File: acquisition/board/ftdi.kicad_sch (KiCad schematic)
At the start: 2 parts, among them U10 FT232HL, U6 ICE40UP5K_QFN48

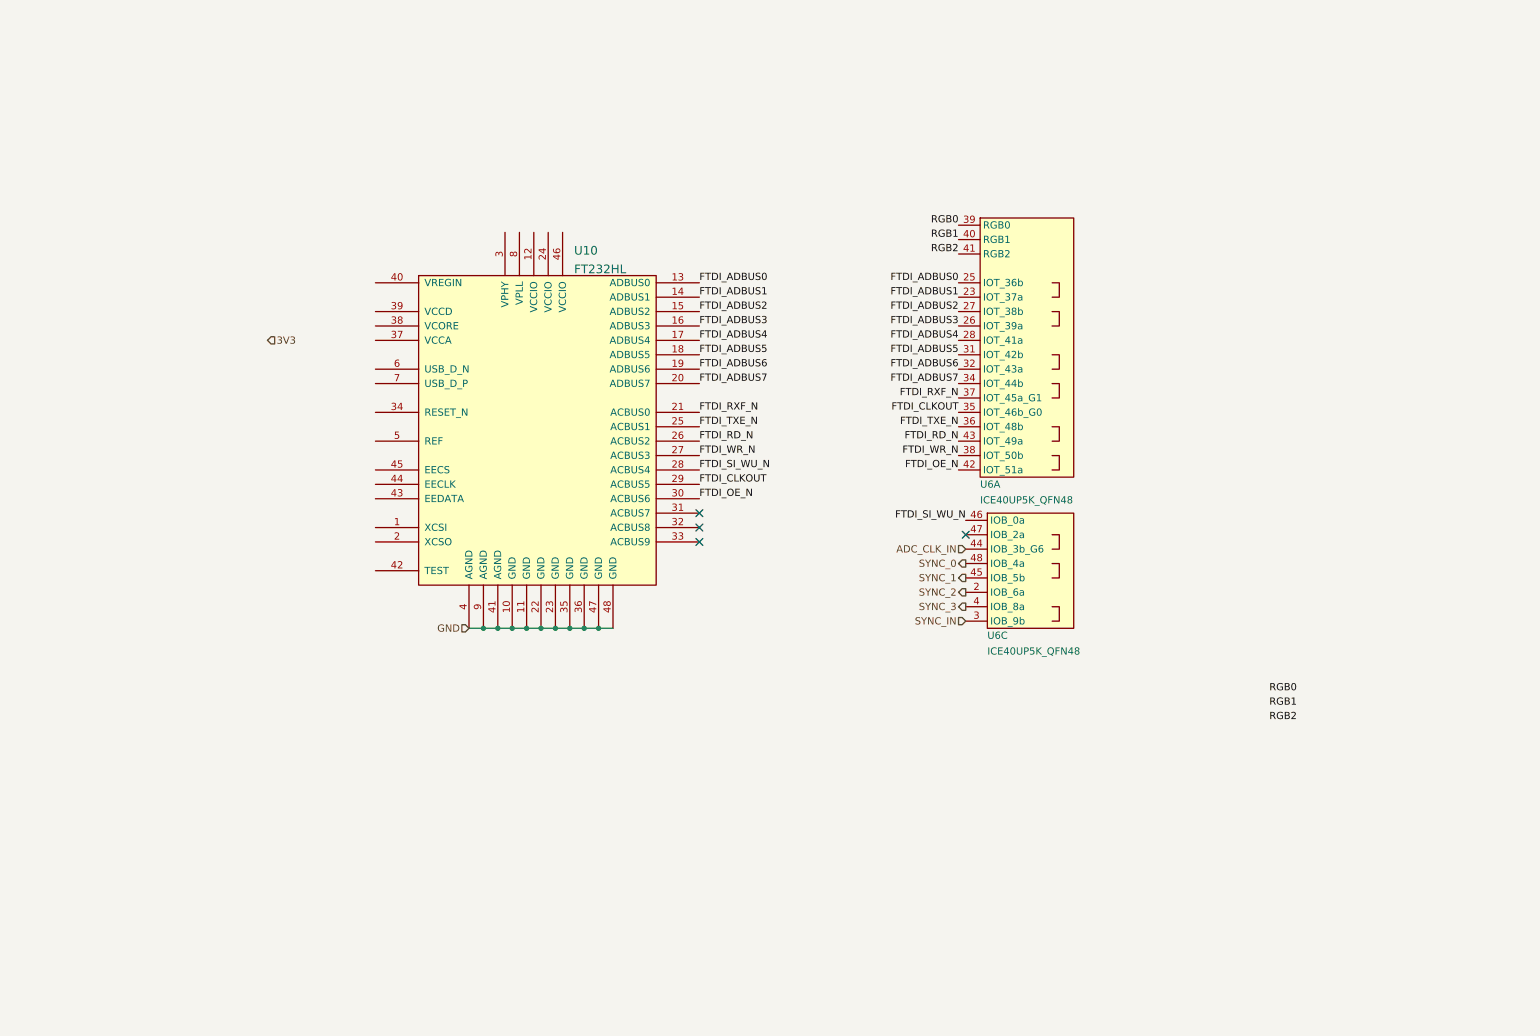
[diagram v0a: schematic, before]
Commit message: Updated schematic with a lot of level shifting and support stuff, power decoupling, etc. Almost done except power supply and protection diodes
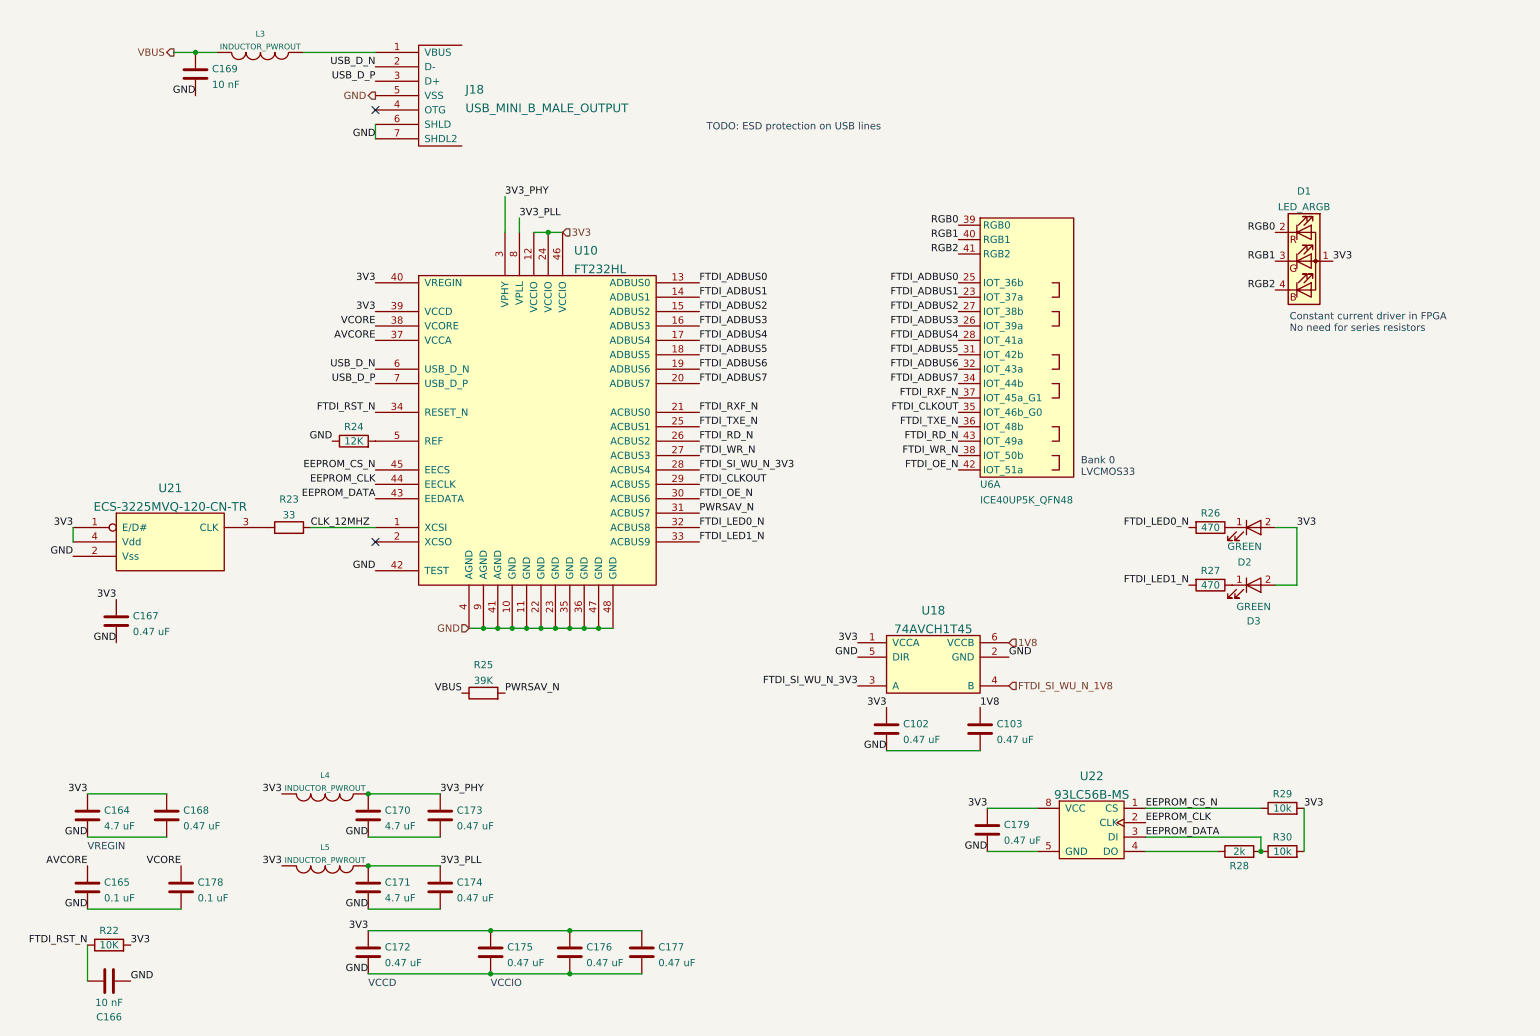
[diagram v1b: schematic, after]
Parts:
- removed unit 3 of U6
- added C102, C103, C167, C168, C172, C173, C174, C175, C176, C177, C179: 0.47 uF, symbol device:C
- added C164, C170, C171: 4.7 uF, symbol device:C
- added C165, C178: 0.1 uF, symbol device:C
- added C166, C169: 10 nF, symbol device:C
- added D1: LED_ARGB, symbol device:LED_ARGB
- added D2, D3: GREEN, symbol device:LED
- added J18: USB_MINI_B_MALE_OUTPUT, symbol special-azonenberg:USB_MINI_B_MALE_OUTPUT
- added L3, L4, L5: INDUCTOR_PWROUT, symbol passive-azonenberg:INDUCTOR_PWROUT
- added R22: 10K, symbol device:R
- added R23: 33, symbol device:R
- added R24: 12K, symbol device:R
- added R25: 39K, symbol device:R
- added R26, R27: 470, symbol device:R
- added R28: 2k, symbol device:R
- added R29, R30: 10k, symbol device:R
- added U18: 74AVCH1T45, symbol special-azonenberg:74LVC1T45
- added U21: ECS-3225MVQ-120-CN-TR, symbol osc-azonenberg:OSC
- added U22: 93LC56B-MS, symbol memory-azonenberg:93LC56B-MS
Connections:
- net 3V3: now also U10.12 (VCCIO), U10.24 (VCCIO), U10.39 (VCCD), U10.40 (VREGIN), U10.46 (VCCIO), C102.1, C164.1, C167.1, C168.1, C172.1, C175.1, C176.1, C177.1, C179.1, D1.1 (A), D2.2 (A), D3.2 (A), L4.2, L5.2, R22.2, R29.2, R30.2, U18.1 (VCCA), U21.1 (E/D#), U21.4 (Vdd), U22.8 (VCC)
- net GND: now also U10.42 (TEST), C102.2, C103.2, C164.2, C165.2, C166.2, C167.2, C168.2, C169.2, C170.2, C171.2, C172.2, C173.2, C174.2, C175.2, C176.2, C177.2, C178.2, C179.2, J18.5 (VSS), J18.6 (SHLD), J18.7 (SHDL2), R24.1, U18.2 (GND), U18.5 (DIR), U21.2 (Vss), U22.5 (GND)
- net RGB0: now also D1.2 (RK)
- net RGB1: now also D1.3 (GK)
- net RGB2: now also D1.4 (BK)
- net CLK_12MHZ: now reaches U10.1 (XCSI)
- net CLK_12MHZ: now also R23.2
- net 3V3_PHY: now reaches U10.3 (VPHY)
- net 3V3_PHY: now also C170.1, C173.1, L4.1
- net PWRSAV_N: now reaches U10.31 (ACBUS7)
- net PWRSAV_N: now also R25.2
- net FTDI_LED0_N: now reaches U10.32 (ACBUS8)
- net FTDI_LED0_N: now also R26.2
- net FTDI_LED1_N: now reaches U10.33 (ACBUS9)
- net FTDI_LED1_N: now also R27.2
- net FTDI_RST_N: now reaches U10.34 (RESET_N)
- net FTDI_RST_N: now also C166.1, R22.1
- net AVCORE: now reaches U10.37 (VCCA)
- net AVCORE: now also C165.1
- net VCORE: now reaches U10.38 (VCORE)
- net VCORE: now also C178.1
- net EEPROM_DATA: now reaches U10.43 (EEDATA)
- net EEPROM_DATA: now also R28.2, R30.1, U22.3 (DI)
- net EEPROM_CLK: now reaches U10.44 (EECLK)
- net EEPROM_CLK: now also U22.2 (CLK)
- net EEPROM_CS_N: now reaches U10.45 (EECS)
- net EEPROM_CS_N: now also R29.1, U22.1 (CS)
- net at U10.5 (REF): now also R24.2
- net USB_D_N: now reaches U10.6 (USB_D_N)
- net USB_D_N: now also J18.2 (D-)
- net USB_D_P: now reaches U10.7 (USB_D_P)
- net USB_D_P: now also J18.3 (D+)
- net 3V3_PLL: now reaches U10.8 (VPLL)
- net 3V3_PLL: now also C171.1, C174.1, L5.1
- net FTDI_SI_WU_N renamed FTDI_SI_WU_N_3V3
- net FTDI_SI_WU_N_3V3: now also U18.3 (A)
- new net: D2.1 (K), R26.1
- new net: R23.1, U21.3 (CLK)
- new net: R28.1, U22.4 (DO)
- new net: J18.1 (VBUS), L3.1
- new net: D3.1 (K), R27.1
- new net 1V8: C103.1, U18.6 (VCCB)
- new net FTDI_SI_WU_N_1V8: U18.4 (B)
- new net VBUS: C169.1, L3.2, R25.1
- no-connect marks 4 -> 2
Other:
- note added: "Bank 0 LVCMOS33"
- note added: "Constant current driver in FPGA No need for series resistors"
- note added: "TODO: ESD protection on USB lines"
- note added: "VCCD"
- note added: "VCCIO"
- note added: "VREGIN"

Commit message: Lots of progress on power supply design, added a bunch of test points, etc
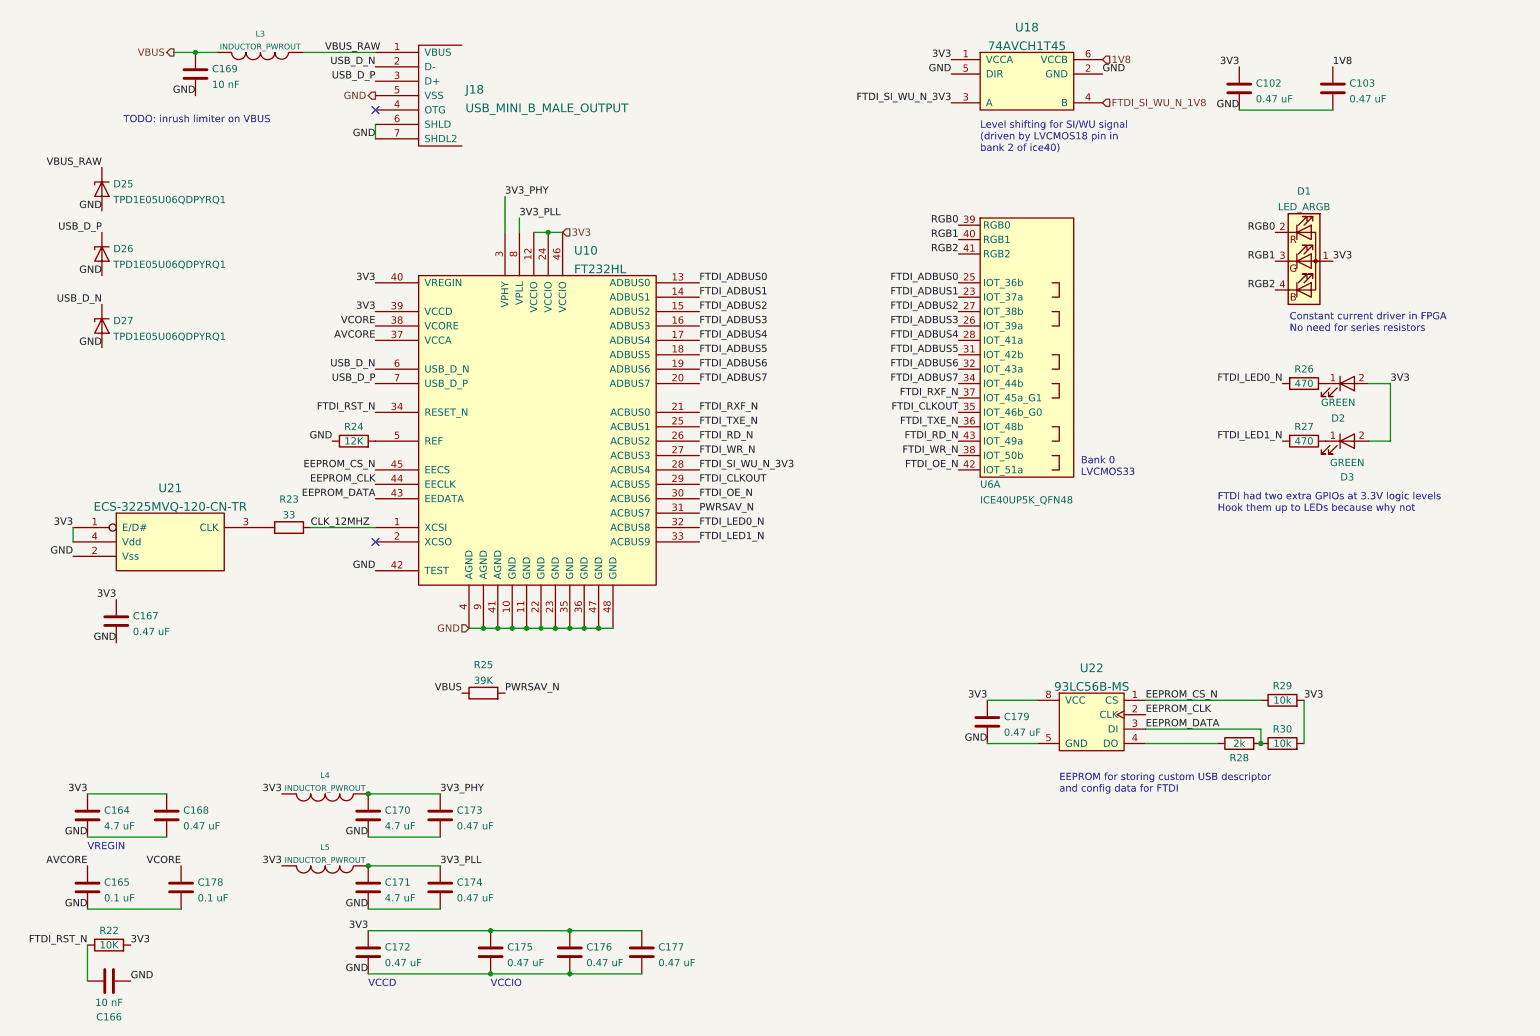
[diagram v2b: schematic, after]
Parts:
- added D25, D26, D27: TPD1E05U06QDPYRQ1, symbol device:D_Zener
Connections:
- net GND: now also D25.2 (A), D26.2 (A), D27.2 (A)
- net USB_D_N: now also D27.1 (K)
- net USB_D_P: now also D26.1 (K)
- net VBUS_RAW: now reaches J18.1 (VBUS), L3.1
- net VBUS_RAW: now also D25.1 (K)
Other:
- note added: "EEPROM for storing custom USB descriptor and config data for FTDI"
- note added: "FTDI had two extra GPIOs at 3.3V logic levels Hook them up to LEDs because why not"
- note added: "Level shifting for SI/WU signal (driven by LVCMOS18 pin in bank 2 of ice40)"
- note added: "TODO: inrush limiter on VBUS"
- note removed: "TODO: ESD protection on USB lines"
- moved on the sheet: C102, C103, C179, D2, D3, R26, R27, R28, R29, R30, U18, U22

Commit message: More power supply work, added PLL loop filter, soft start, began assigning footprints
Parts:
- removed J18: USB_MINI_B_MALE_OUTPUT, symbol special-azonenberg:USB_MINI_B_MALE_OUTPUT
- added C220: 4.7 uF, azonenberg_pcb:EIA_0603_CAP_NOSILK, symbol device:C
- added J18: UX60SX-MB-5ST, azonenberg_pcb:CONN_HIROSE_UX60S-MB-5ST_MINI_USB, symbol hirose-azonenberg:HIROSE_UX60SX-MB-5ST_(MINI_USB)
- added U29: SIP32408, symbol power-azonenberg:SIP32408
- C102, C103, C165, C167, C168, C172, C173, C174, C175, C176, C177, C178, C179: footprint (none) -> azonenberg_pcb:EIA_0402_CAP_NOSILK
- L3, L4, L5: value INDUCTOR_PWROUT -> FERRITE
- R22, R23, R26, R27, R29, R30: footprint (none) -> azonenberg_pcb:EIA_0402_RES_NOSILK
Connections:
- net GND: now also C220.2, J18.5 (VSS), J18.6 (SHLD), J18.7 (SHDL2), U29.2 (GND), U29.PAD (GND)
- net USB_D_N: now also J18.2 (D-)
- net USB_D_P: now also J18.3 (D+)
- net VBUS: now also U29.4 (OUT); no longer L3.2
- net VBUS_RAW: now also L3.2, J18.1 (VBUS); no longer L3.1
- new net VBUS_FILT: C220.1, L3.1, U29.1 (IN), U29.3 (EN)
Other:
- note added: "Inrush limiter 2.5 ms turn-on ramp"
- note removed: "TODO: inrush limiter on VBUS"
- moved on the sheet: C169, L3

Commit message: Completed schematic after design review, ready for layout
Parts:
- added R85, R86, R87, R88: 33, azonenberg_pcb:EIA_0402_RES_NOSILK, symbol device:R
- C164, C166, C169, C170, C171: footprint (none) -> azonenberg_pcb:EIA_0603_CAP_NOSILK
- R24, R25, R28: footprint (none) -> azonenberg_pcb:EIA_0402_RES_NOSILK
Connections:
- net FTDI_CLKOUT: now also R88.2; no longer U10.29 (ACBUS5)
- net FTDI_OE_N: now also R87.1; no longer U6.42 (IOT_51a)
- net FTDI_RD_N: now also R85.1; no longer U6.43 (IOT_49a)
- net FTDI_WR_N: now also R86.1; no longer U6.38 (IOT_50b)
- new net: R85.2, U6.43 (IOT_49a)
- new net: R86.2, U6.38 (IOT_50b)
- new net: R87.2, U6.42 (IOT_51a)
- new net: R88.1, U10.29 (ACBUS5)
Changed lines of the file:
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@@
   (title_block
     (title "Digitizer board")
-    (date "2022-07-08")
+    (date "2022-07-17")
     (rev "0.1")
     (company "A. Zonenberg")
@@
     (stroke (width 0) (type default) (color 0 0 0 0))
   )
+  (wire (pts (xy 144.78 96.52) (xy 148.59 96.52))
+    (stroke (width 0) (type default) (color 0 0 0 0))
+  )
   (wire (pts (xy 110.49 52.07) (xy 113.03 52.07))
     (stroke (width 0) (type default) (color 0 0 0 0))
@@
     (stroke (width 0) (type default) (color 0 0 0 0))
   )
+  (wire (pts (xy 170.18 88.9) (xy 175.26 88.9))
+    (stroke (width 0) (type default) (color 0 0 0 0))
+  )
   (wire (pts (xy 215.9 142.24) (xy 228.6 142.24))
     (stroke (width 0) (type default) (color 0 0 0 0))
@@
     (stroke (width 0) (type default) (color 0 0 0 0))
   )
+  (wire (pts (xy 170.18 91.44) (xy 175.26 91.44))
+    (stroke (width 0) (type default) (color 0 0 0 0))
+  )
   (wire (pts (xy 187.96 134.62) (xy 196.85 134.62))
     (stroke (width 0) (type default) (color 0 0 0 0))
   )
   (wire (pts (xy 78.74 158.75) (xy 91.44 158.75))
+    (stroke (width 0) (type default) (color 0 0 0 0))
+  )
+  (wire (pts (xy 170.18 93.98) (xy 175.26 93.98))
     (stroke (width 0) (type default) (color 0 0 0 0))
   )
@@
     (effects (font (size 1.27 1.27)) (justify left bottom))
   )
-  (label "FTDI_RD_N" (at 182.88 88.9 180)
+  (label "FTDI_RD_N" (at 170.18 88.9 180)
     (effects (font (size 1.27 1.27)) (justify right bottom))
   )
@@
     (effects (font (size 1.27 1.27)) (justify right bottom))
   )
-  (label "FTDI_CLKOUT" (at 137.16 96.52 0)
+  (label "FTDI_CLKOUT" (at 148.59 96.52 0)
     (effects (font (size 1.27 1.27)) (justify left bottom))
   )
@@
     (effects (font (size 1.27 1.27)) (justify right bottom))
   )
-  (label "FTDI_WR_N" (at 182.88 91.44 180)
+  (label "FTDI_WR_N" (at 170.18 91.44 180)
     (effects (font (size 1.27 1.27)) (justify right bottom))
   )
@@
     (effects (font (size 1.27 1.27)) (justify left bottom))
   )
-  (label "FTDI_OE_N" (at 182.88 93.98 180)
+  (label "FTDI_OE_N" (at 170.18 93.98 180)
     (effects (font (size 1.27 1.27)) (justify right bottom))
   )
@@
     (pin "5")
     (pin "8")
+  )
+  (symbol (lib_id "device:R") (at 179.07 88.9 90) (unit 1)
+    (in_bom yes) (on_board yes)
+    (property "Reference" "R85" (id 0) (at 171.45 87.63 90))
+    (property "Value" "33" (id 1) (at 179.07 88.9 90))
+    (property "Footprint" "azonenberg_pcb:EIA_0402_RES_NOSILK" (id 2) (at 179.07 90.678 90)
+      (effects (font (size 1.27 1.27)) hide)
+    )
+    (property "Datasheet" "" (id 3) (at 179.07 88.9 0)
+      (effects (font (size 1.27 1.27)) hide)
+    )
+    (pin "1")
+    (pin "2")
   )
   (symbol (lib_id "lattice-azonenberg:ICE40UP5K_QFN48") (at 186.69 95.25 0) (unit 1)
@@
       (effects (font (size 1.27 1.27)) (justify left))
     )
-    (property "Footprint" "" (id 2) (at 79.7052 171.45 0)
+    (property "Footprint" "azonenberg_pcb:EIA_0603_CAP_NOSILK" (id 2) (at 79.7052 171.45 0)
       (effects (font (size 1.27 1.27)) hide)
     )
     (property "Datasheet" "" (id 3) (at 78.74 167.64 0)
+      (effects (font (size 1.27 1.27)) hide)
+    )
+    (pin "1")
+    (pin "2")
+  )
+  (symbol (lib_id "device:R") (at 179.07 91.44 90) (unit 1)
+    (in_bom yes) (on_board yes)
+    (property "Reference" "R86" (id 0) (at 171.45 90.17 90))
+    (property "Value" "33" (id 1) (at 179.07 91.44 90))
+    (property "Footprint" "azonenberg_pcb:EIA_0402_RES_NOSILK" (id 2) (at 179.07 93.218 90)
+      (effects (font (size 1.27 1.27)) hide)
+    )
+    (property "Datasheet" "" (id 3) (at 179.07 91.44 0)
       (effects (font (size 1.27 1.27)) hide)
     )
@@
       (effects (font (size 1.27 1.27)) (justify left))
     )
-    (property "Footprint" "" (id 2) (at 109.5248 27.94 0)
+    (property "Footprint" "azonenberg_pcb:EIA_0603_CAP_NOSILK" (id 2) (at 109.5248 27.94 0)
       (effects (font (size 1.27 1.27)) hide)
     )
@@
     (property "Reference" "R24" (id 0) (at 76.2 86.36 90))
     (property "Value" "12K" (id 1) (at 76.2 88.9 90))
-    (property "Footprint" "" (id 2) (at 76.2 90.678 90)
+    (property "Footprint" "azonenberg_pcb:EIA_0402_RES_NOSILK" (id 2) (at 76.2 90.678 90)
       (effects (font (size 1.27 1.27)) hide)
     )
@@
     (property "Reference" "R25" (id 0) (at 99.06 128.3675 90))
     (property "Value" "39K" (id 1) (at 99.06 131.1426 90))
-    (property "Footprint" "" (id 2) (at 99.06 135.128 90)
+    (property "Footprint" "azonenberg_pcb:EIA_0402_RES_NOSILK" (id 2) (at 99.06 135.128 90)
       (effects (font (size 1.27 1.27)) hide)
     )
@@
       (effects (font (size 1.27 1.27)) (justify left))
     )
-    (property "Footprint" "" (id 2) (at 30.1752 158.75 0)
+    (property "Footprint" "azonenberg_pcb:EIA_0603_CAP_NOSILK" (id 2) (at 30.1752 158.75 0)
       (effects (font (size 1.27 1.27)) hide)
     )
@@
     (pin "2")
   )
+  (symbol (lib_id "device:R") (at 179.07 93.98 90) (unit 1)
+    (in_bom yes) (on_board yes)
+    (property "Reference" "R87" (id 0) (at 171.45 92.71 90))
+    (property "Value" "33" (id 1) (at 179.07 93.98 90))
+    (property "Footprint" "azonenberg_pcb:EIA_0402_RES_NOSILK" (id 2) (at 179.07 95.758 90)
+      (effects (font (size 1.27 1.27)) hide)
+    )
+    (property "Datasheet" "" (id 3) (at 179.07 93.98 0)
+      (effects (font (size 1.27 1.27)) hide)
+    )
+    (pin "1")
+    (pin "2")
+  )
   (symbol (lib_id "device:C") (at 78.74 154.94 0) (unit 1)
     (in_bom yes) (on_board yes) (fields_autoplaced)
@@
       (effects (font (size 1.27 1.27)) (justify left))
     )
-    (property "Footprint" "" (id 2) (at 79.7052 158.75 0)
+    (property "Footprint" "azonenberg_pcb:EIA_0603_CAP_NOSILK" (id 2) (at 79.7052 158.75 0)
       (effects (font (size 1.27 1.27)) hide)
     )
@@
     (pin "2")
   )
+  (symbol (lib_id "device:R") (at 140.97 96.52 90) (unit 1)
+    (in_bom yes) (on_board yes)
+    (property "Reference" "R88" (id 0) (at 147.32 95.25 90))
+    (property "Value" "33" (id 1) (at 140.97 96.52 90))
+    (property "Footprint" "azonenberg_pcb:EIA_0402_RES_NOSILK" (id 2) (at 140.97 98.298 90)
+      (effects (font (size 1.27 1.27)) hide)
+    )
+    (property "Datasheet" "" (id 3) (at 140.97 96.52 0)
+      (effects (font (size 1.27 1.27)) hide)
+    )
+    (pin "1")
+    (pin "2")
+  )
   (symbol (lib_id "device:C") (at 33.02 184.15 90) (unit 1)
     (in_bom yes) (on_board yes)
     (property "Reference" "C166" (id 0) (at 33.02 190.5 90))
     (property "Value" "10 nF" (id 1) (at 33.02 187.96 90))
-    (property "Footprint" "" (id 2) (at 36.83 183.1848 0)
+    (property "Footprint" "azonenberg_pcb:EIA_0603_CAP_NOSILK" (id 2) (at 36.83 183.1848 0)
       (effects (font (size 1.27 1.27)) hide)
     )
@@
     (property "Reference" "R28" (id 0) (at 232.41 144.78 90))
     (property "Value" "2k" (id 1) (at 232.41 142.24 90))
-    (property "Footprint" "" (id 2) (at 232.41 144.018 90)
-      (effects (font (size 1.27 1.27)) hide)
-    )
+    (property "Footprint" "azonenberg_pcb:EIA_0402_RES_NOSILK" (id 2) (at 232.41 144.018 90)
+      (effects (font (size 1.27 1.27)) hide)
+    )
